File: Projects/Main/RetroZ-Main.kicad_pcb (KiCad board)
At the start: 2 copper layers, 100 x 80 mm, 22 parts, among them J1 PJ-102A, J2 Master Bus, SW1 On/Off, SW2 RESET, U1 74HCT04, U2 L7805CV-DG, U3 Z80CPU, U4 max699cpa, Y1 7.3728Mhz

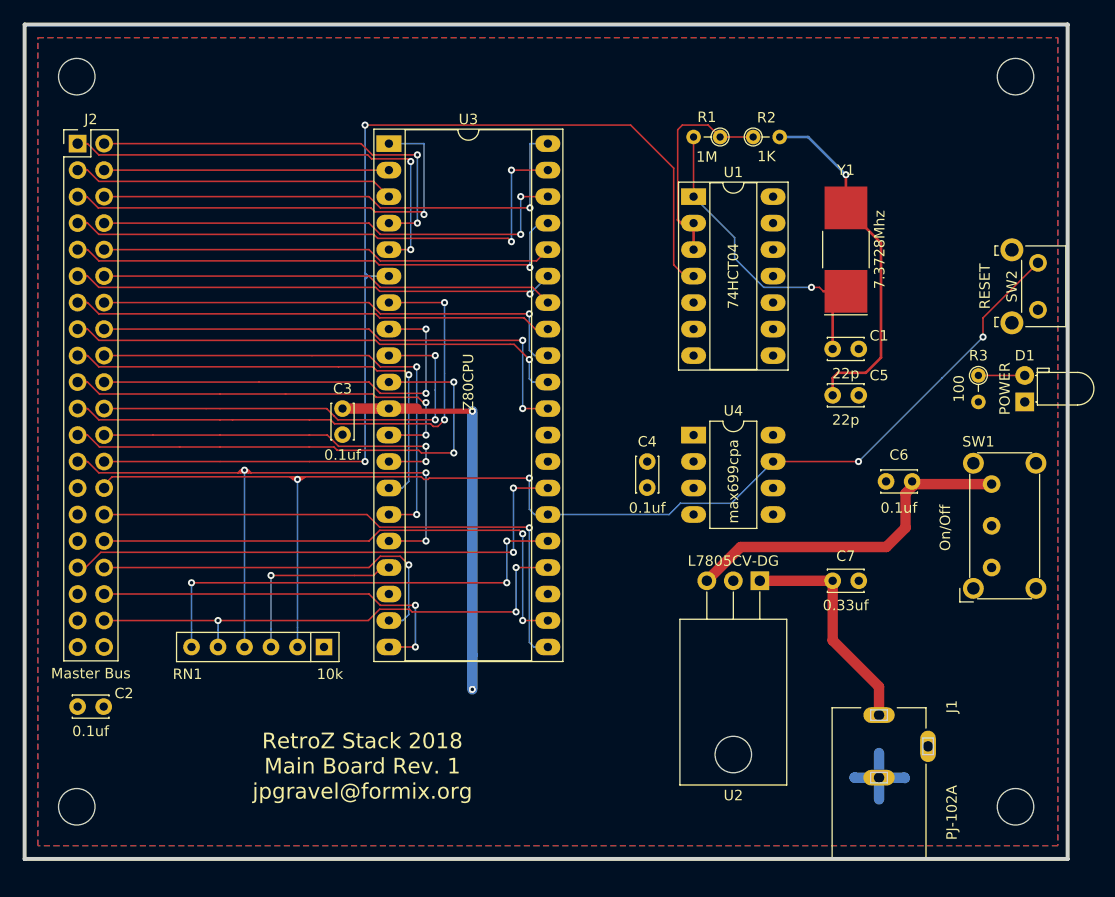
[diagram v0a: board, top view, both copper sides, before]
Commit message: restructuration du dossier de projet
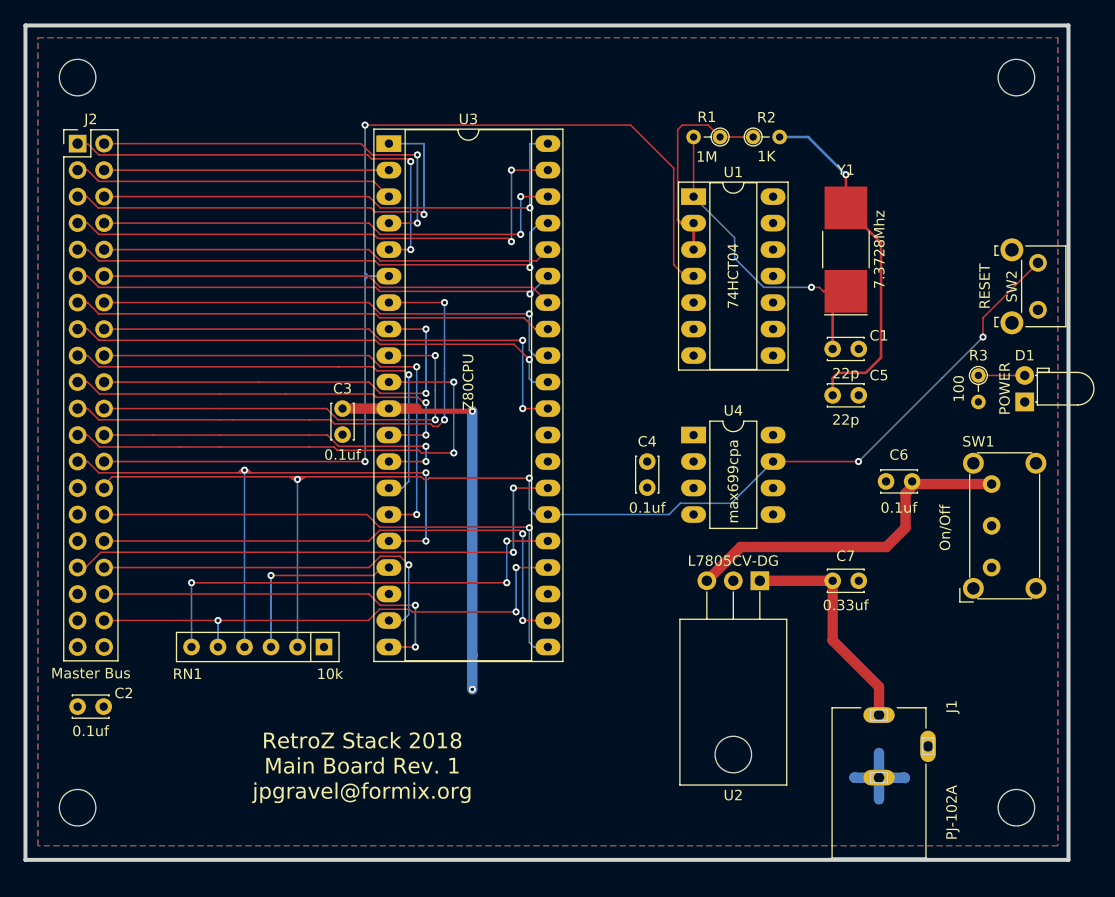
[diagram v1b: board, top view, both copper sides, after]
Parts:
- moved REF** 0.12 mm to (90.2, 137.2)
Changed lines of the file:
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@@
     (links 80)
     (no_connects 0)
-    (area 0 0 0 0)
+    (area 89.7676 49.8726 196.807401 145.8074)
     (thickness 1.6)
     (drawings 1)
@@
   )
   (module EuroBoard_Outline:EuroBoard_halb_Type-I_100mmX80mm_holes (layer Top)
-    (at 90.17 137.16)
+    (at 90.25 137.25)
     (descr "Outline, Eurocard 1/2, Type I, 100x80mm, with holes 3,5mm")
     (tags "Outline, Eurocard 1/2, Type I, 100x80mm, with holes 3,5mm")
@@
   (segment (start 125.095 99.06) (end 128.143 99.06) (width 0.1524) (layer Top) (net 28))
   (segment (start 128.651 99.06) (end 128.143 99.06) (width 0.1524) (layer Top) (net 28))
-  (segment (start 111.252 116.84) (end 111.252 115.2525) (width 0.1524) (layer Bottom) (net 29) (status 400000))
+  (segment (start 111.252 116.84) (end 111.252 115.2525) (width 0.1524) (layer Bottom) (net 29))
   (segment (start 111.252 115.2525) (end 111.252 99.8855) (width 0.1524) (layer Bottom) (net 29))
   (via (at 111.252 99.8855) (size 0.6858) (drill 0.3302) (layers Top Bottom) (net 29))
@@
   (segment (start 122.809 80.9625) (end 122.809 81.28) (width 0.1524) (layer Bottom) (net 30))
   (segment (start 97.79 99.06) (end 97.79 99.06) (width 0.254) (layer Top) (net 30))
-  (segment (start 116.332 116.84) (end 116.332 114.9985) (width 0.1524) (layer Bottom) (net 31) (status 400000))
+  (segment (start 116.332 116.84) (end 116.332 114.9985) (width 0.1524) (layer Bottom) (net 31))
   (segment (start 116.332 114.9985) (end 116.332 100.7745) (width 0.1524) (layer Bottom) (net 31))
   (via (at 116.332 100.7745) (size 0.6858) (drill 0.3302) (layers Top Bottom) (net 31))
@@
   (segment (start 124.2695 112.8395) (end 127.635 112.8395) (width 0.1524) (layer Top) (net 36))
   (segment (start 123.19 111.76) (end 124.2695 112.8395) (width 0.1524) (layer Top) (net 36))
-  (segment (start 108.712 116.84) (end 108.712 115.2525) (width 0.1524) (layer Bottom) (net 37) (status 400000))
+  (segment (start 108.712 116.84) (end 108.712 115.2525) (width 0.1524) (layer Bottom) (net 37))
   (via (at 108.712 114.3) (size 0.6858) (drill 0.3302) (layers Top Bottom) (net 37))
   (segment (start 108.712 115.2525) (end 108.712 114.3) (width 0.1524) (layer Bottom) (net 37))
@@
   (segment (start 172.085 120.65) (end 167.64 116.205) (width 1) (layer Top) (net 41))
   (segment (start 160.655 110.49) (end 167.64 110.49) (width 1) (layer Top) (net 41))
-  (segment (start 113.792 116.84) (end 113.792 115.1255) (width 0.1524) (layer Bottom) (net 43) (status 400000))
+  (segment (start 113.792 116.84) (end 113.792 115.1255) (width 0.1524) (layer Bottom) (net 43))
   (via (at 113.792 109.982) (size 0.6858) (drill 0.3302) (layers Top Bottom) (net 43))
   (segment (start 113.792 109.982) (end 121.793 109.982) (width 0.1524) (layer Top) (net 43))
@@
   (segment (start 113.792 115.1255) (end 113.792 109.982) (width 0.1524) (layer Bottom) (net 43))
   (segment (start 124.3965 109.22) (end 125.095 109.22) (width 0.1524) (layer Top) (net 43))
-  (segment (start 106.172 116.84) (end 106.172 115.1255) (width 0.1524) (layer Bottom) (net 44) (status 400000))
+  (segment (start 106.172 116.84) (end 106.172 115.1255) (width 0.1524) (layer Bottom) (net 44))
   (via (at 106.172 110.6805) (size 0.6858) (drill 0.3302) (layers Top Bottom) (net 44))
   (segment (start 106.172 110.6805) (end 136.398 110.6805) (width 0.1524) (layer Top) (net 44))

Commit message: sio2+ctc
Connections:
- J2 pad 27: Net-(J2-Pad27) -> ~NMI
- J2 pad 35: Net-(J2-Pad35) -> ~BUSRQ
- J2 pad 37: Net-(J2-Pad37) -> ~BUSACK
- RN1 pad 3: Net-(RN1-Pad3) -> ~NMI
- RN1 pad 6: Net-(RN1-Pad6) -> ~BUSRQ
- U3 pad 17: Net-(RN1-Pad3) -> ~NMI
- U3 pad 23: Net-(U3-Pad23) -> ~BUSACK
- U3 pad 25: Net-(RN1-Pad6) -> ~BUSRQ
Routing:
- net ~BUSRQ: track 0.00 -> 55.8 mm, vias 0 -> 3
- net ~BUSACK: track 0.00 -> 53.6 mm, vias 0 -> 1
- net ~NMI: track 0.00 -> 44.7 mm, vias 0 -> 2
- net Net-(RN1-Pad6): track 44.3 -> 0.00 mm, vias 3 -> 0
- net Net-(RN1-Pad3): track 18.5 -> 0.00 mm, vias 1 -> 0

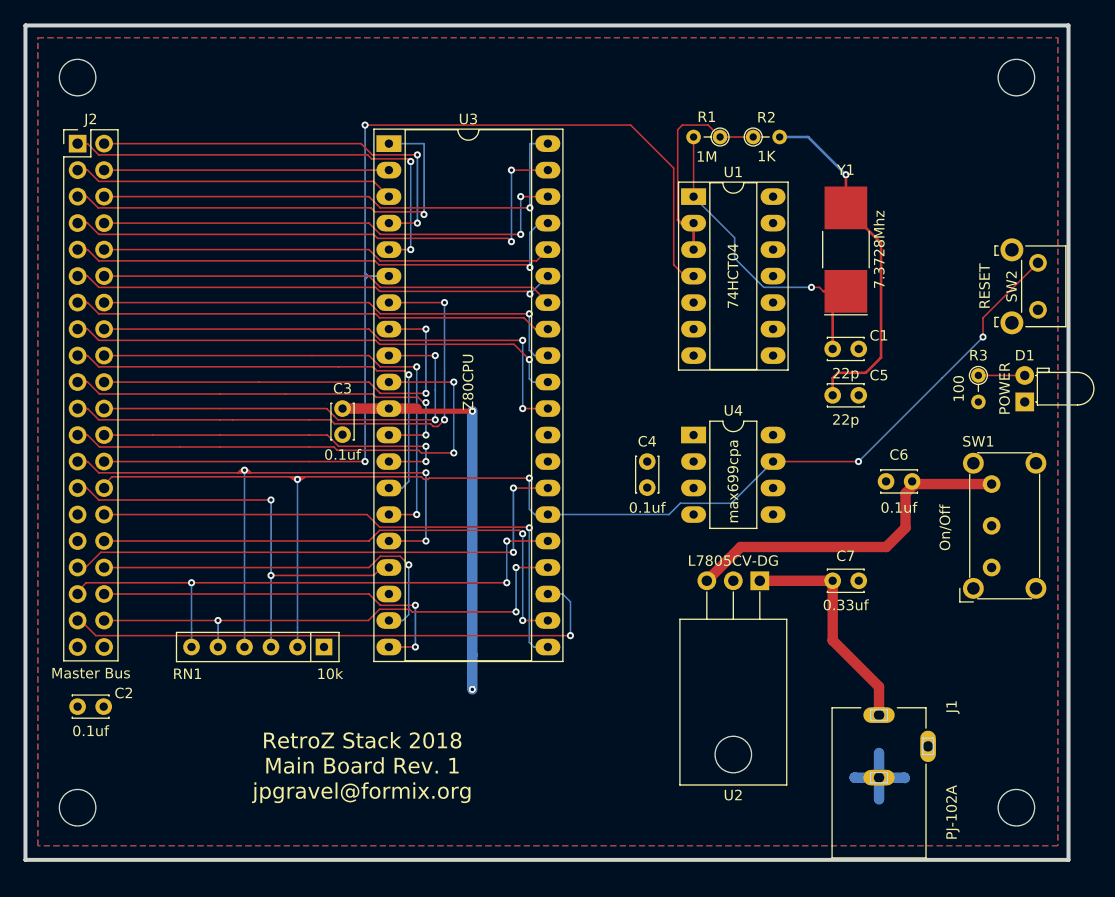
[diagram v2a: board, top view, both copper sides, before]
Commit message: added usb to serial with an FT230XS-U chip
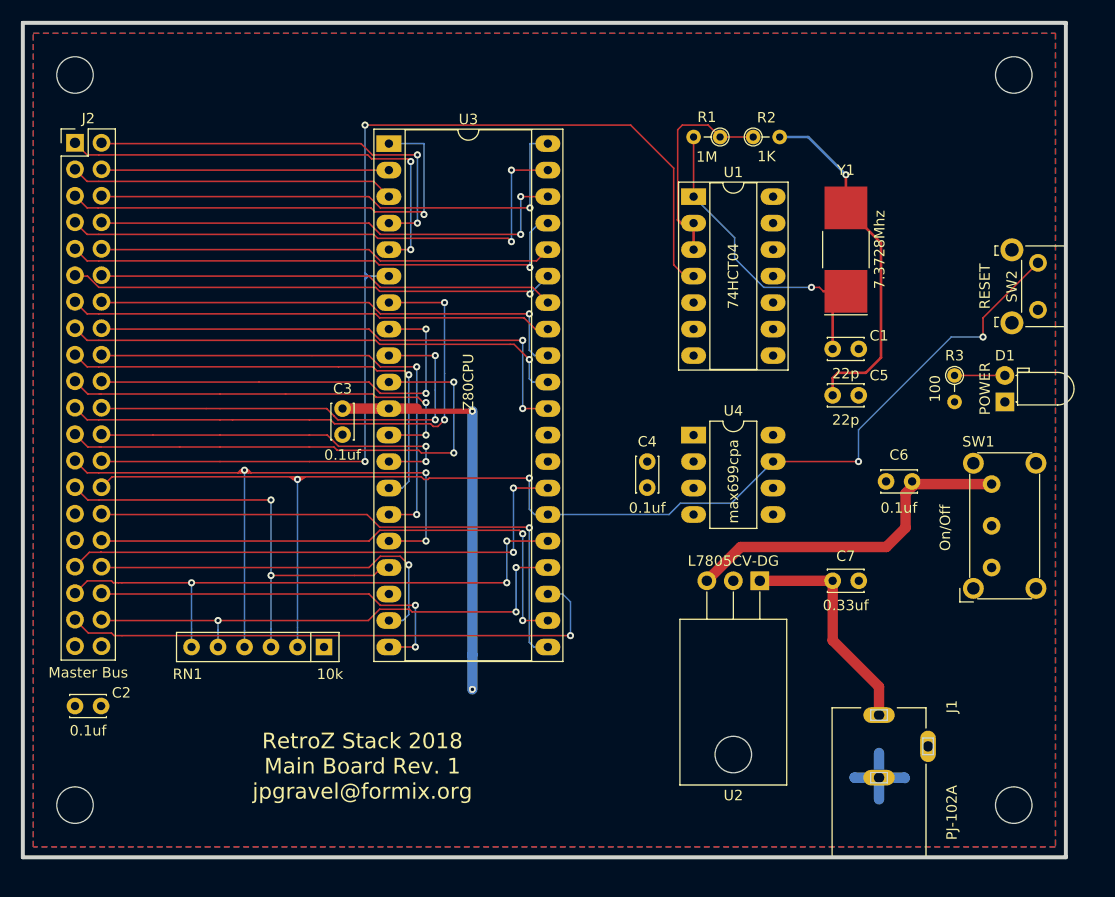
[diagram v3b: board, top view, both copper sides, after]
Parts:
- moved R3 2.29 mm to (179.3, 90.8)
- moved D1 1.91 mm to (184.2, 93.3)
- moved REF** 0.35 mm to (90.0, 137.0)
- moved J2 0.26 mm to (95.0, 68.5)
- moved C2 0.26 mm to (95.0, 122.5)
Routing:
- net ~RESET: track 123.7 -> 125.5 mm

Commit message: fixed Processor Board
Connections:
- J2 pad 27: ~NMI -> Net-(J2-Pad27)
- RN1 pad 3: ~NMI -> Net-(RN1-Pad3)
- U3 pad 17: ~NMI -> Net-(RN1-Pad3)
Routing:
- net ~NMI: track 45.0 -> 0.00 mm, vias 2 -> 0
- net Net-(RN1-Pad3): track 0.00 -> 18.5 mm, vias 0 -> 1
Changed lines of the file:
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@@
 (kicad_pcb (version 4) (host pcbnew 4.0.7)
   (general
-    (links 83)
+    (links 82)
     (no_connects 0)
-    (area 89.5976 49.7126 196.807401 145.6474)
+    (area 0 0 0 0)
     (thickness 1.6)
     (drawings 1)
-    (tracks 453)
+    (tracks 447)
     (zones 0)
     (modules 22)
-    (nets 53)
+    (nets 54)
   )
   (page USLetter)
@@
   (net 50 ~BUSRQ)
   (net 51 ~BUSACK)
-  (net 52 ~NMI)
+  (net 52 "Net-(J2-Pad27)")
+  (net 53 "Net-(RN1-Pad3)")
   (net_class Default "This is the default net class."
     (clearance 0.1524)
@@
     (add_net "Net-(D1-Pad2)")
     (add_net "Net-(J1-Pad3)")
+    (add_net "Net-(J2-Pad27)")
     (add_net "Net-(J2-Pad29)")
     (add_net "Net-(J2-Pad31)")
     (add_net "Net-(R1-Pad1)")
+    (add_net "Net-(RN1-Pad3)")
     (add_net "Net-(SW1-Pad1)")
     (add_net "Net-(U3-Pad18)")
@@
     (add_net ~M1)
     (add_net ~MREQ)
-    (add_net ~NMI)
     (add_net ~RD)
     (add_net ~RESET)
@@
       (net 14 /A6))
     (pad 17 thru_hole oval (at 0 40.64) (size 2.4 1.6) (drill 0.8) (layers *.Cu *.Mask)
-      (net 52 ~NMI))
+      (net 53 "Net-(RN1-Pad3)"))
     (pad 37 thru_hole oval (at 15.24 7.62) (size 2.4 1.6) (drill 0.8) (layers *.Cu *.Mask)
       (net 13 /A7))
@@
       (net 30 CLK))
     (pad 27 thru_hole oval (at 0 33.02) (size 1.7 1.7) (drill 1) (layers *.Cu *.Mask)
-      (net 52 ~NMI))
+      (net 52 "Net-(J2-Pad27)"))
     (pad 28 thru_hole oval (at 2.54 33.02) (size 1.7 1.7) (drill 1) (layers *.Cu *.Mask)
       (net 31 ~RESET))
@@
       (net 31 ~RESET))
     (pad 3 thru_hole oval (at 5.08 0 180) (size 1.6 1.6) (drill 0.8) (layers *.Cu *.Mask)
-      (net 52 ~NMI))
+      (net 53 "Net-(RN1-Pad3)"))
     (pad 4 thru_hole oval (at 7.62 0 180) (size 1.6 1.6) (drill 0.8) (layers *.Cu *.Mask)
       (net 29 ~INT))
@@
   (segment (start 99.1805 110.6805) (end 98.6805 110.6805) (width 0.1524) (layer Top) (net 50))
   (segment (start 98.5 110.5) (end 96.18 110.5) (width 0.1524) (layer Top) (net 50))
-  (segment (start 95 111.68) (end 96.18 110.5) (width 0.1524) (layer Top) (net 50) (status 400000))
+  (segment (start 95 111.68) (end 96.18 110.5) (width 0.1524) (layer Top) (net 50))
   (segment (start 99.5 110.6805) (end 106.172 110.6805) (width 0.1524) (layer Top) (net 50))
   (segment (start 99.5 110.6805) (end 99.1805 110.6805) (width 0.1524) (layer Top) (net 50))
@@
   (via (at 142.5 115.75) (size 0.6858) (drill 0.3302) (layers Top Bottom) (net 51))
   (segment (start 99.5 115.75) (end 142.5 115.75) (width 0.1524) (layer Top) (net 51))
-  (segment (start 96.28 115.5) (end 95 114.22) (width 0.1524) (layer Top) (net 51) (status 800000))
+  (segment (start 96.28 115.5) (end 95 114.22) (width 0.1524) (layer Top) (net 51))
   (segment (start 98.5 115.5) (end 96.28 115.5) (width 0.1524) (layer Top) (net 51))
   (segment (start 98.75 115.75) (end 98.5 115.5) (width 0.1524) (layer Top) (net 51))
-  (segment (start 97.282 102.743) (end 96.223 102.743) (width 0.1524) (layer Top) (net 52))
-  (segment (start 97.282 102.743) (end 113.792 102.743) (width 0.1524) (layer Top) (net 52))
-  (via (at 113.792 102.743) (size 0.6858) (drill 0.3302) (layers Top Bottom) (net 52))
-  (segment (start 113.792 109.982) (end 113.792 102.743) (width 0.1524) (layer Bottom) (net 52))
-  (segment (start 96.223 102.743) (end 95 101.52) (width 0.1524) (layer Top) (net 52))
-  (segment (start 113.792 116.84) (end 113.792 115.1255) (width 0.1524) (layer Bottom) (net 52))
-  (via (at 113.792 109.982) (size 0.6858) (drill 0.3302) (layers Top Bottom) (net 52))
-  (segment (start 113.792 109.982) (end 121.793 109.982) (width 0.1524) (layer Top) (net 52))
-  (segment (start 121.793 109.982) (end 123.6345 109.982) (width 0.1524) (layer Top) (net 52))
-  (segment (start 123.6345 109.982) (end 124.3965 109.22) (width 0.1524) (layer Top) (net 52))
-  (segment (start 113.792 115.1255) (end 113.792 109.982) (width 0.1524) (layer Bottom) (net 52))
-  (segment (start 124.3965 109.22) (end 125.095 109.22) (width 0.1524) (layer Top) (net 52))
+  (segment (start 123.19 109.982) (end 124.333 109.982) (width 0.1524) (layer Top) (net 53))
+  (via (at 113.792 109.982) (size 0.6858) (drill 0.3302) (layers Top Bottom) (net 53))
+  (segment (start 113.792 109.982) (end 121.8565 109.982) (width 0.1524) (layer Top) (net 53))
+  (segment (start 121.8565 109.982) (end 123.19 109.982) (width 0.1524) (layer Top) (net 53))
+  (segment (start 113.792 116.84) (end 113.792 109.982) (width 0.1524) (layer Bottom) (net 53) (status 400000))
+  (segment (start 124.333 109.982) (end 125.095 109.22) (width 0.1524) (layer Top) (net 53) (status 800000))
   (zone (net 3) (net_name VCC) (layer Top) (hatch edge 0.508)
     (connect_pads (clearance 0.508))
